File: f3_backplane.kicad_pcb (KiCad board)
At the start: 4 copper layers, 95.8 x 74 mm, 50 parts, among them J1 PCIEx4_HOST, J2 Bus_M.2_Socket_M, J3 SATA_Backplane, J4 SATA_Backplane, Q1 MMBT3904, U1 NCP45521, U2 NCP45521, U3 NCP45521, U4 NCP45521

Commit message: Add datasheet links and digikey part numbers
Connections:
- J2 pad 52: /NVMe SSD/CLKREQ# -> unconnected-(J2-~{CLKREQ}-Pad52)
- J2 pad 54: /NVMe SSD/PEWAKE# -> unconnected-(J2-~{PEWAKE}-Pad54)

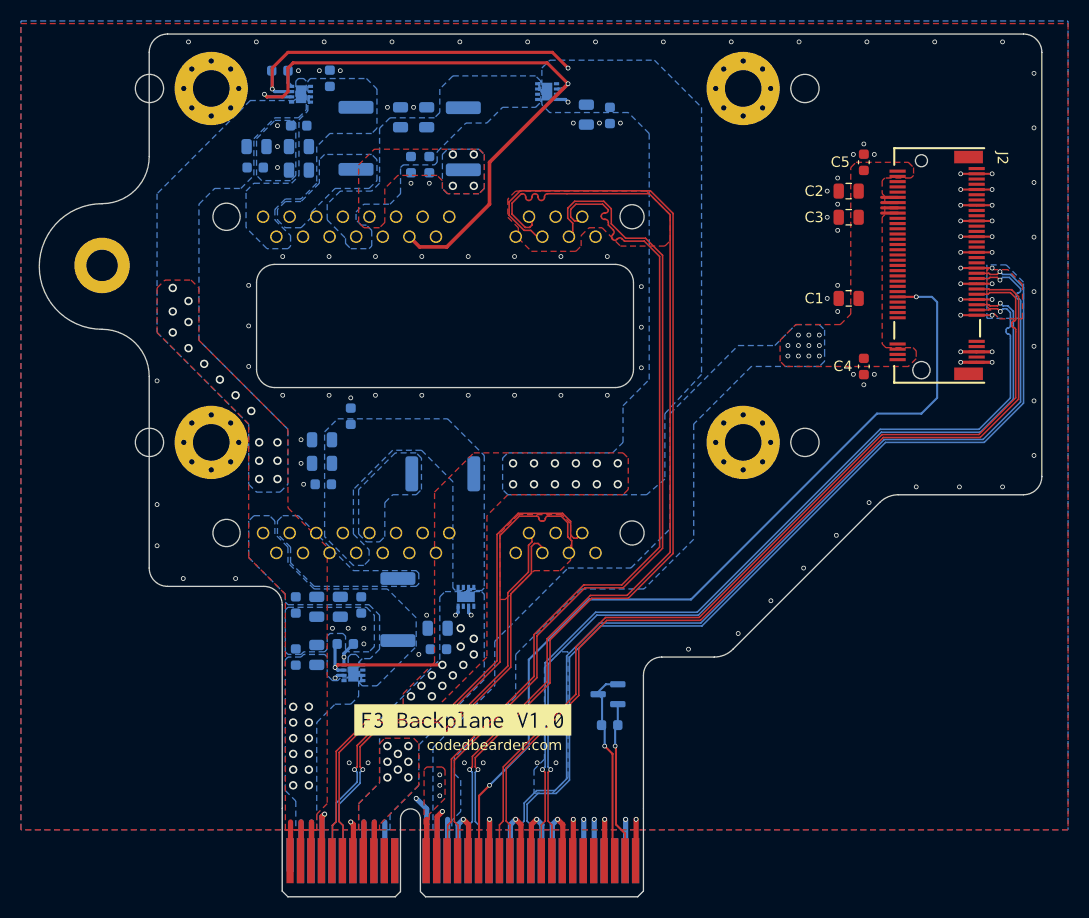
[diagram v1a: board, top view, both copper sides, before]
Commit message: Improve differential pair intra-pair matching
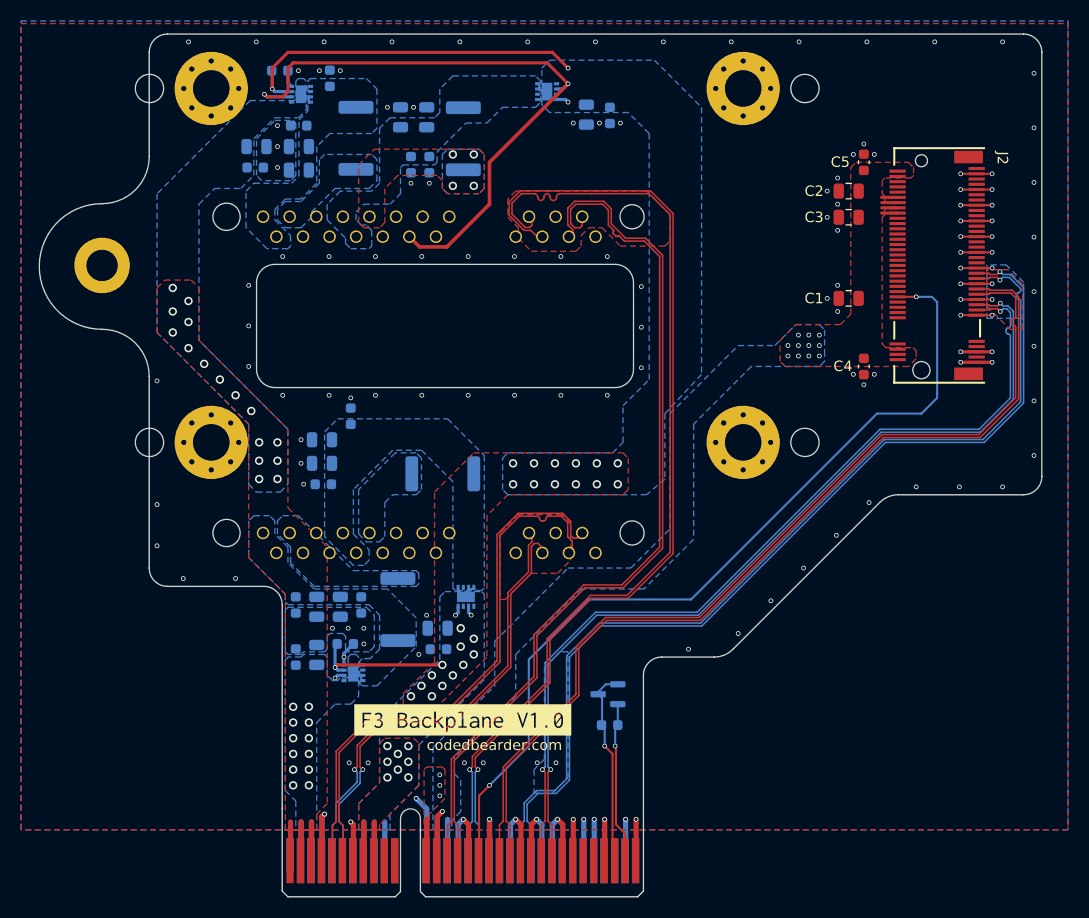
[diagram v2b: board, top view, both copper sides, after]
